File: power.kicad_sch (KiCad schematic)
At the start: 45 parts, among them J2 B3B-XH-A, U5 EG11752, U6 BQ25606RGER, U9 ME6211C33M5G

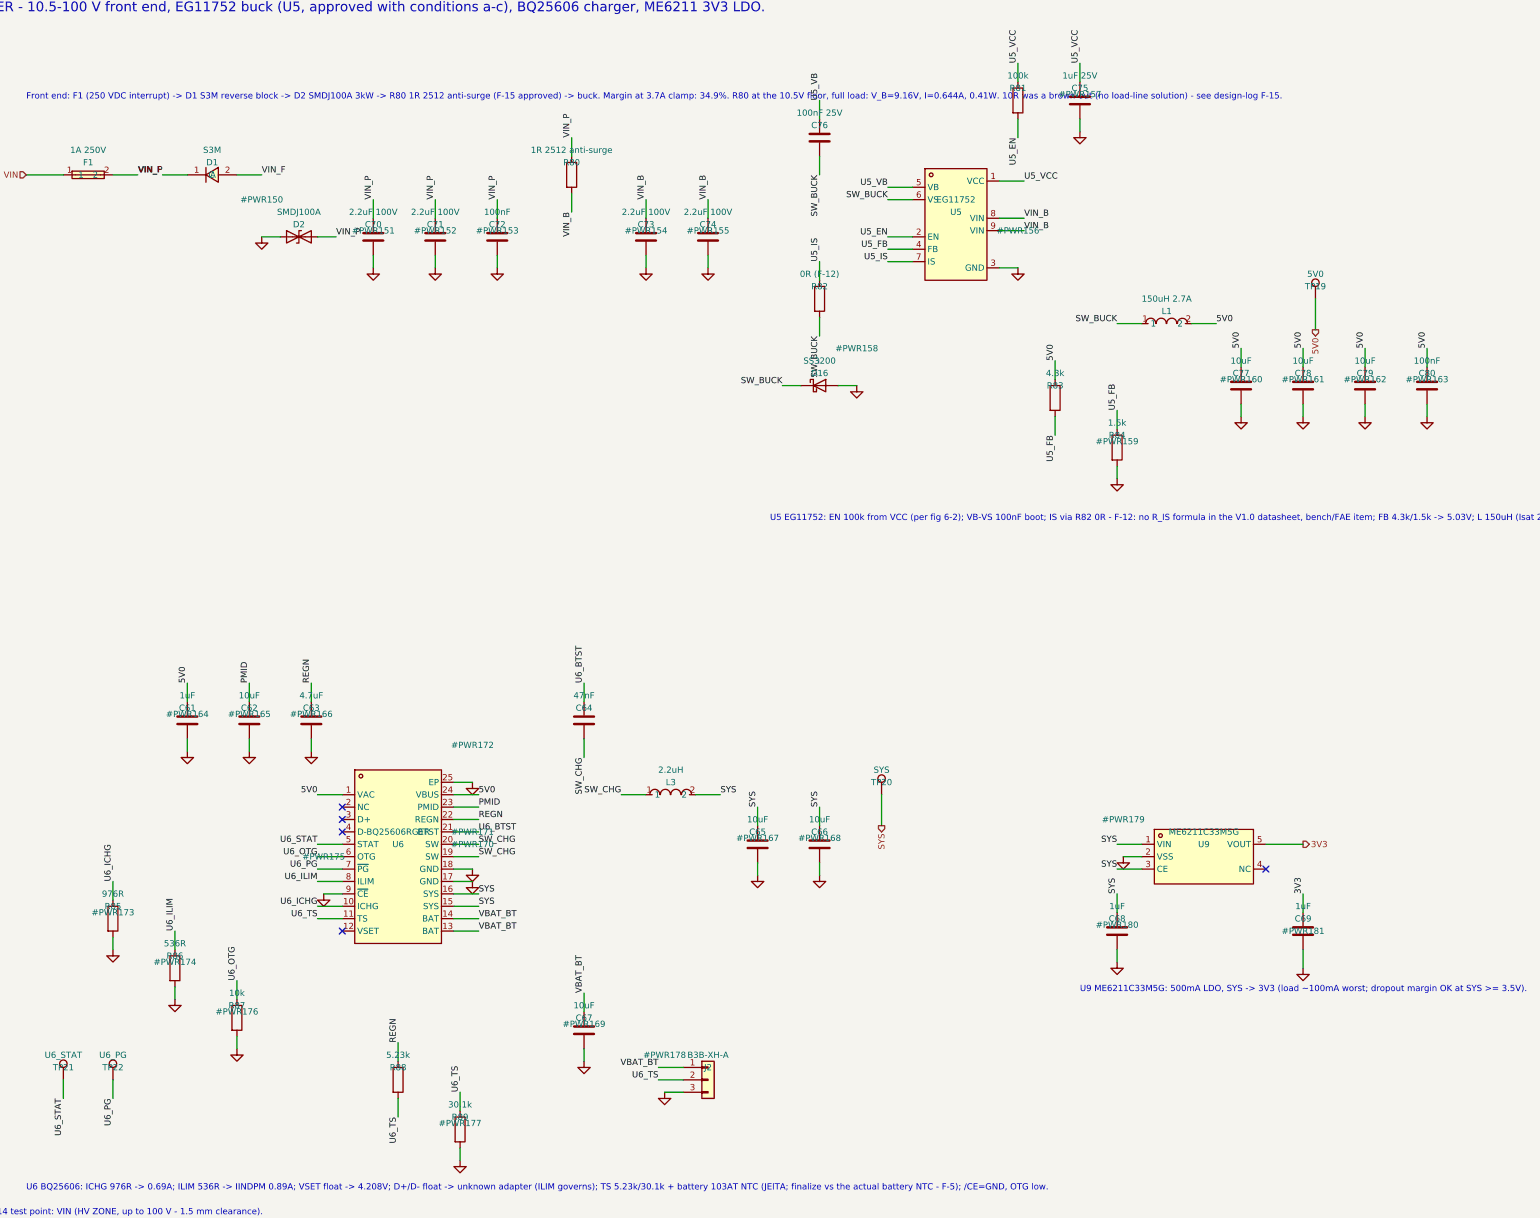
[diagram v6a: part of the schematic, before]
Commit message: Pre-routing: R90 short protection, bias-T on all builds, F-23 antenna temp
Bias-T POPULATED on all builds - the selected GNSS antenna C784386 is active
(LNA 21.5 dB, 1.8-3.6 V), so L4/R90/C83 are no longer DNP. C84 100pF series DC
block was already always-fitted.

R90 antenna-short current limit = 68R 1210 (F-22). The vendor publishes only a
TYPICAL 4.3 mA and no maximum, so this is designed to a conservative multiple:
  normal, 3V3 at -5%: V_ant = 2.84 V at 1x typical, still 1.95 V at 4x typical
                      (needs >= 1.80 V) - tolerates 4.3x the typical current
  fault, 3V3 at +5%:  50.1 mA into a shorted coax, vs a 500 mA LDO already
                      carrying ~150 mA, and L4 rated 320 mA
  P_R90 in fault:     0.171 W, 68% of a 50%-derated 1210
Deliberately more conservative than the ~150 mA brief: 22R would hit 143 mA but
needs a 2512 and burns 0.448 W CONTINUOUSLY inside a sealed IP65 box at 70 C,
from a fault that does not clear itself. C85 10nF added at the injection node
because 68R (vs Quectel's 10R) raises supply-noise coupling into the LNA.

F-23 NEW - the antennas are the weakest thermal link. Both are -45 to +85 C for
OPERATING AND STORAGE (identical ranges, verified verbatim in both datasheets).
That gives 15 C margin at the +70 C operating limit but ZERO margin at the 85 C
survival limit, with no excursion or derating data published by either vendor.
They are lid-mounted, i.e. in the hottest part of the enclosure. Bench soak at
85 C required before release; decision open on whether to accept, narrow the
survival spec, or treat antennas as serviceable.

Antenna retention must be MECHANICAL - heat stake, clamp, rib or captive pocket,
never adhesive alone (Quectel Antenna Design Guide V3.3 3.1 note 3: adhesive
weakens at high ambient). Added to the installation sheet AND as a housing
selection criterion in handoff 6.3 and 7 - the enclosure must provide the
retention feature, so a plain smooth-lidded box will not do.

Also noted: both datashe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
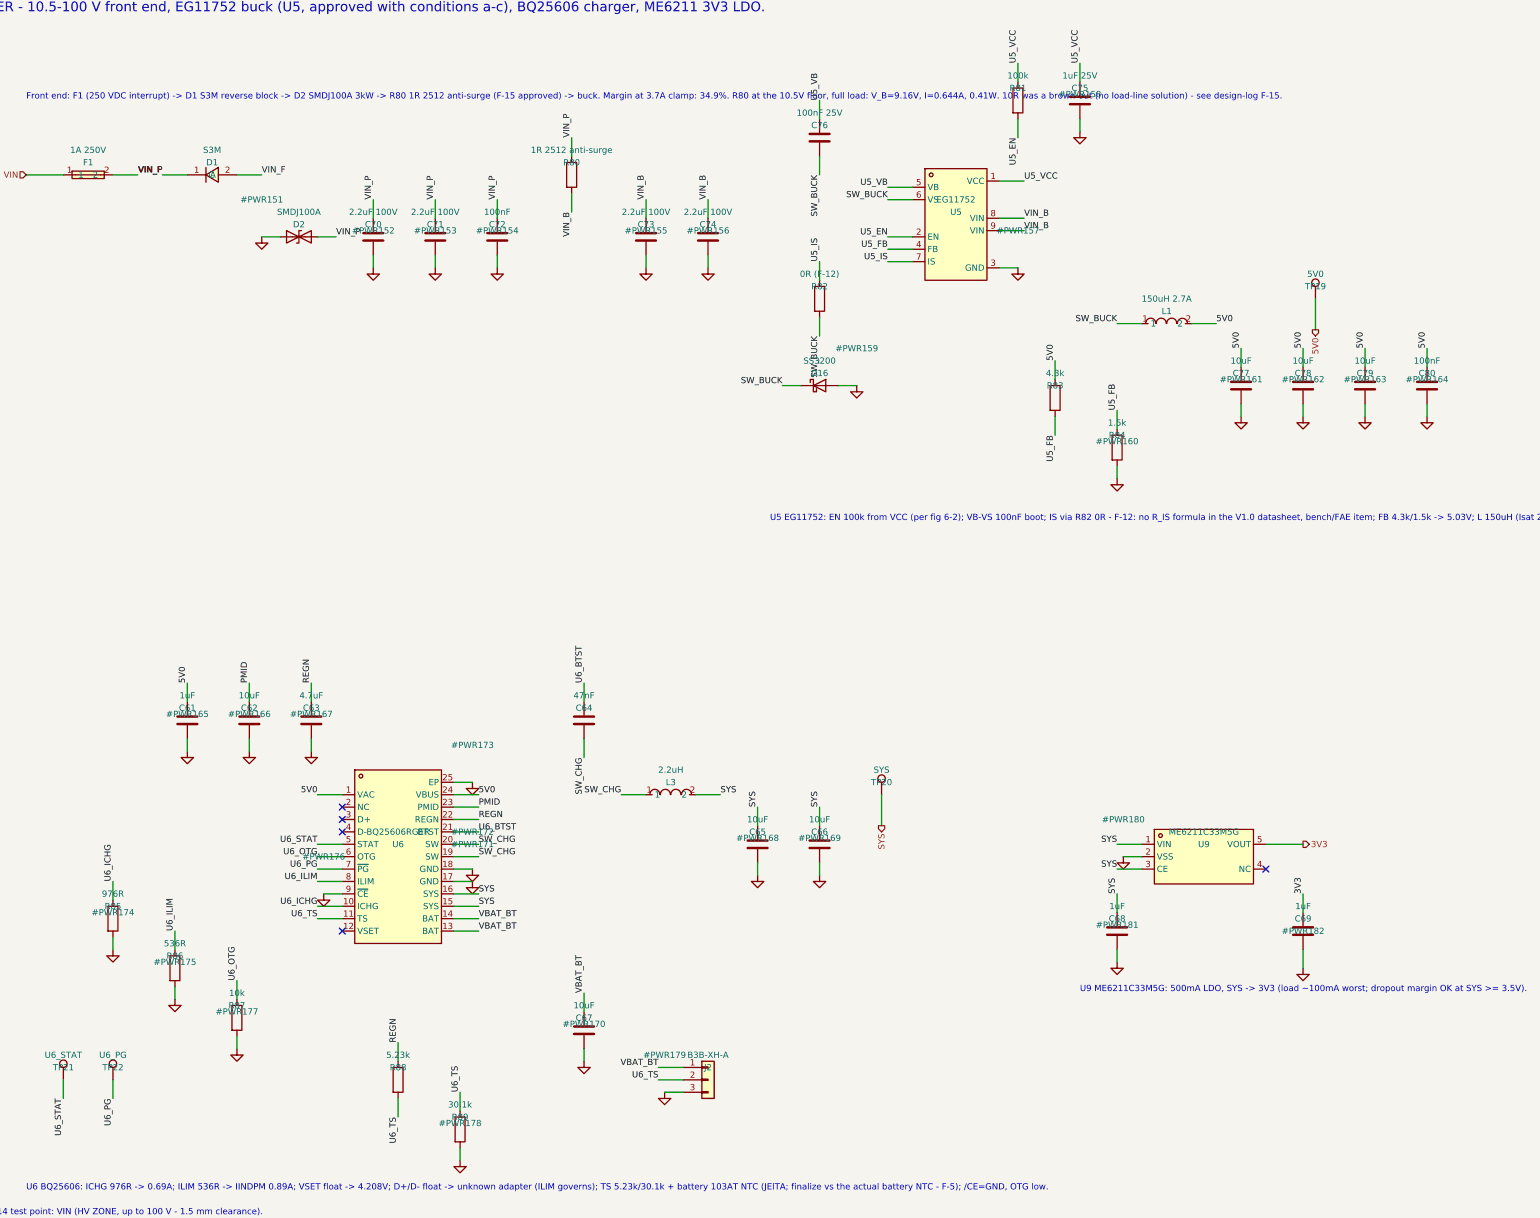
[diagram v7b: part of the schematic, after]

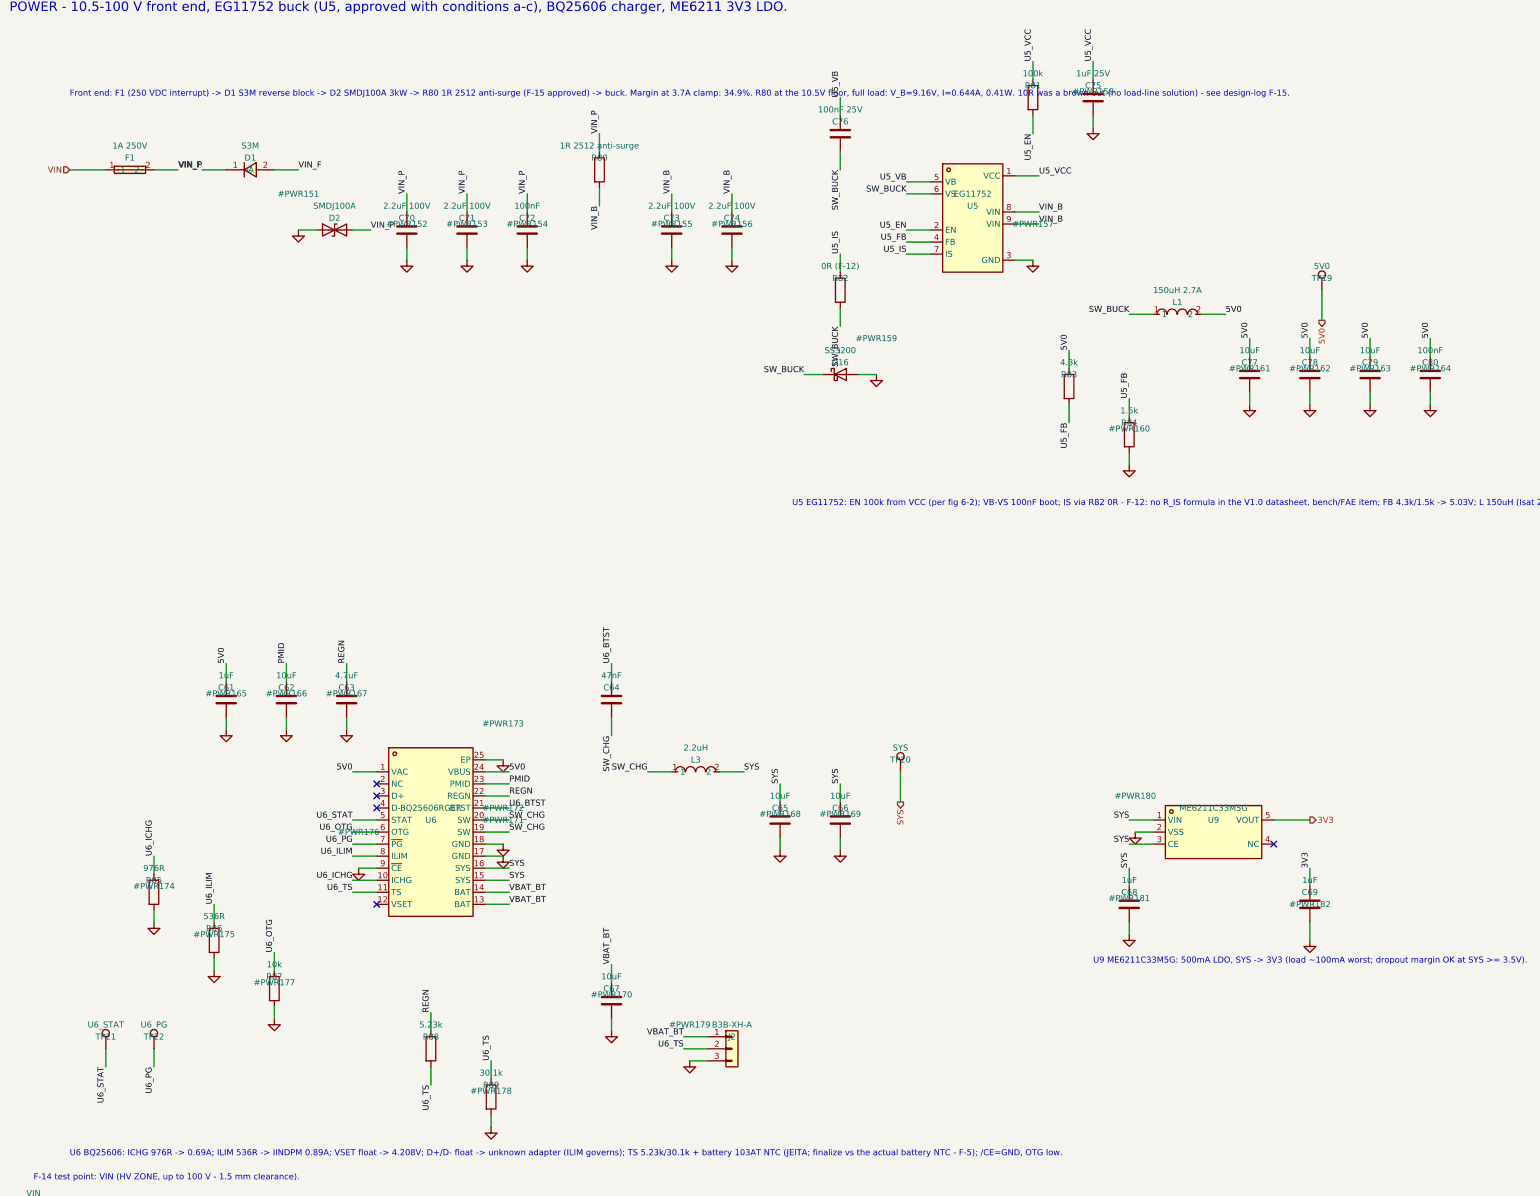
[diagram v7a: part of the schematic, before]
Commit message: Step 1-3: fix rule floors, classify SW_BUCK as HV, shrink, fix HV router
Step 1 - rule mismatch fixed and verified:
  netclasses.py gains BOARD_RULES + _assert_floors(). Every class now meets
  track >= 0.20 mm and via annulus >= 0.10 mm. min_clearance had been silently
  reset to 0.0 by a KiCad round trip; restored to 0.15 and now asserted after
  the round trip so it cannot regress unnoticed. Exported DSN verified to carry
  the values (kicad_default 200, GND 500, MODEM_BULK 2000, RF 400, HV 500/600).

Step 2 - HV hand-routing, and three real defects it uncovered:

  1. /power/SW_BUCK was in the Default netclass. It is the buck switching node:
     it swings from GND to VIN every cycle, so it is a 100 V net with fast
     edges, and it was running at 0.20 mm track / 0.15 mm clearance. U5_VB
     (bootstrap) rides on it and was equally misclassified. Both moved to HV.
     Found because the maze router treated SW_BUCK as LV and threw a 1.50 mm
     halo around U5's own VIN pins, making /power/VIN_B unroutable at 0/4.

  2. HV_ZONE stopped at x = 20.0 and so EXCLUDED the buck primary side. U5 sits
     at x 35.4..42.3 with C73, C74 and D16 beside it, and VIN_B runs 22 mm from
     R80 to reach it. The highest-energy node on the board was outside the HV
     rule area - which also meant the U5 package exception approved under F-20
     was dead code, since it is conditioned on insideArea('HV_ZONE'). HV_ZONE
     is now L-shaped: left strip plus the buck primary.

  3. Three defects in pcbroute_hv.py itself, together responsible for 128 of
     the 129 clearance violations the first routed board had:
       - halos were sized for a 0.50 mm track (half 0.25) but the router also
         drops 0.80 mm vias, so cells legal for a track were illegal for a via
       - halo extents were quantised with round(), letting a cell centre sit up
         to RES/2 = 0.075 mm inside the forbidden region. That is exactly the
         size of the 0.545..0.594 mm shortfalls DRC reporte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
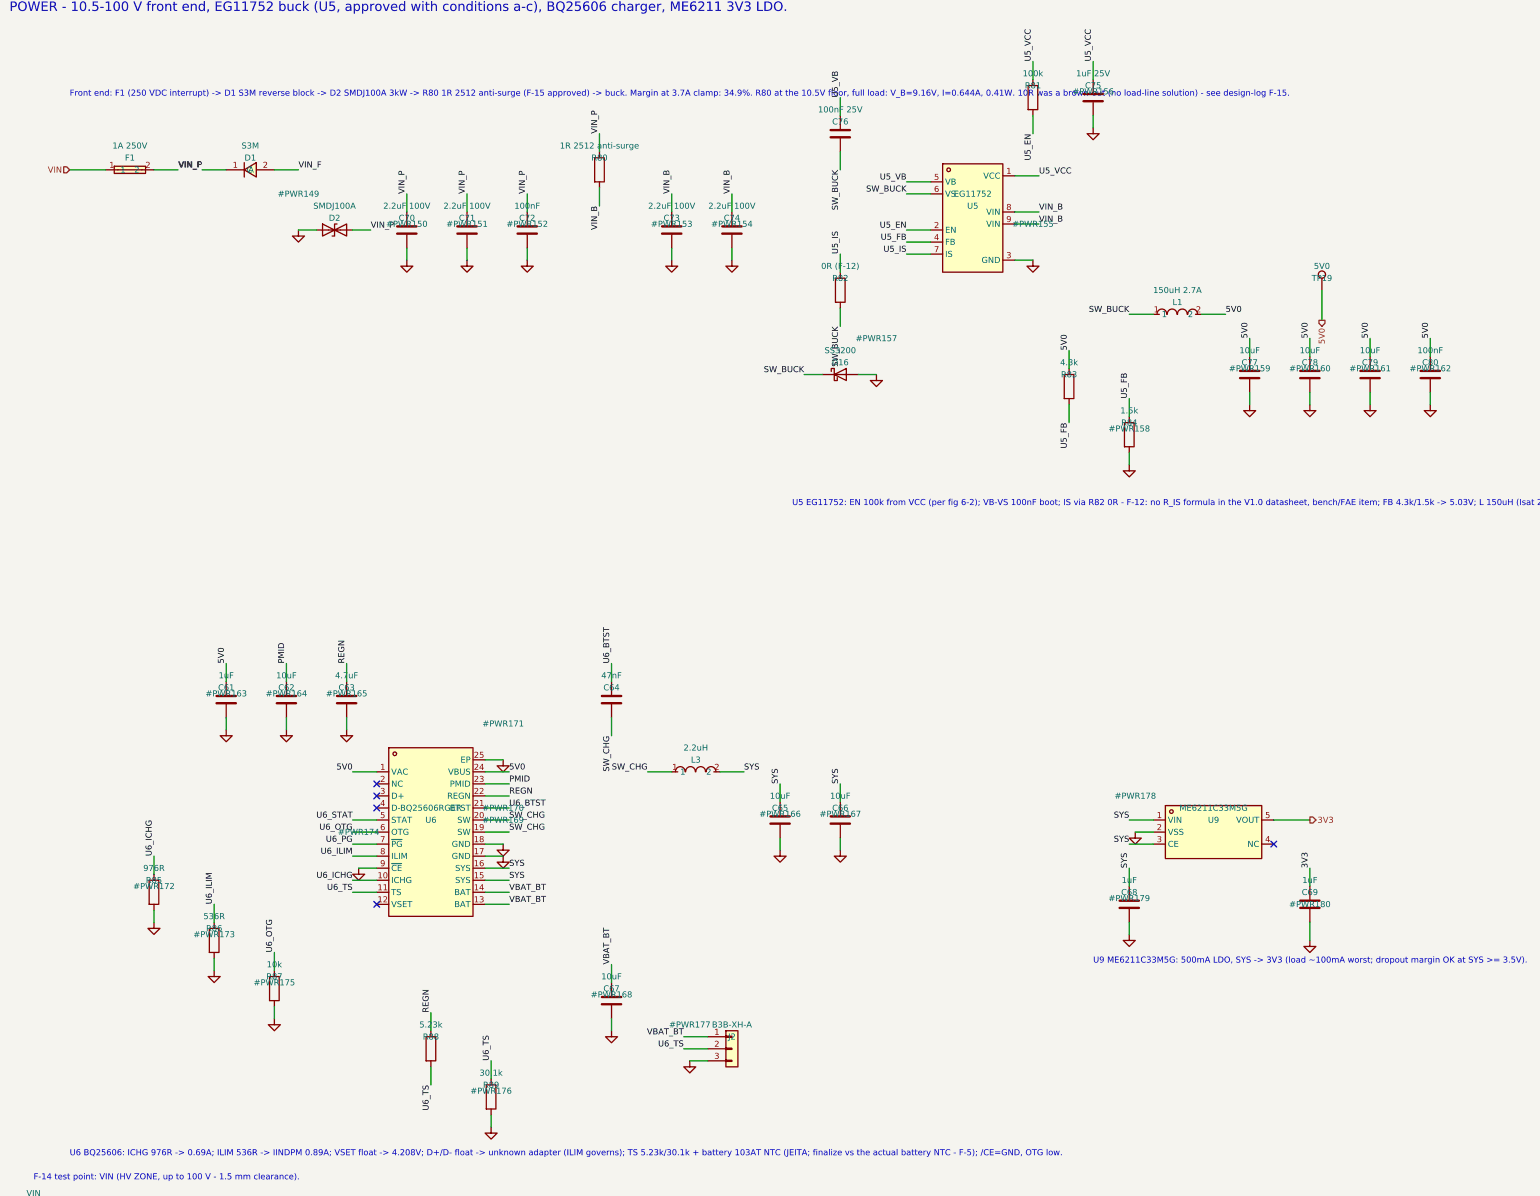
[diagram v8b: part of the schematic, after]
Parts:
- removed TP20: SYS, TestPoint:TestPoint_Pad_D1.5mm, symbol Connector:TestPoint
- removed TP21: U6_STAT, TestPoint:TestPoint_Pad_D1.5mm, symbol Connector:TestPoint
- removed TP22: U6_PG, TestPoint:TestPoint_Pad_D1.5mm, symbol Connector:TestPoint
